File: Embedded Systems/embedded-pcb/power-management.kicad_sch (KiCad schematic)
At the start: 7 parts, among them J2 Screw_Terminal_01x02, U2 LM7805_TO220, U3 LM1117T-3.3

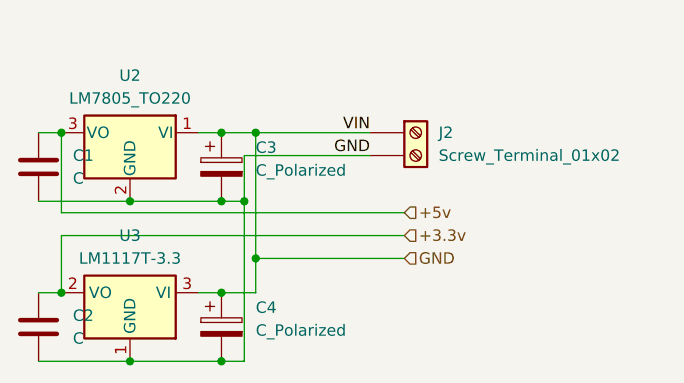
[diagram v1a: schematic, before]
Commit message: feat: finalised PCB
Finalised the electrical design and PCB, including adding a power switch, silksreening, and mounting holes.
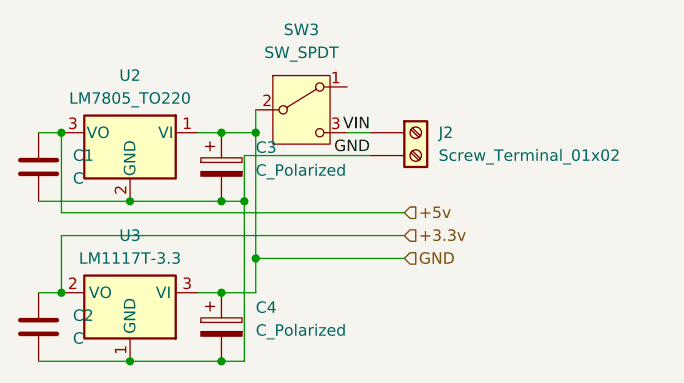
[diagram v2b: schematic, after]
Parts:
- added SW3: SW_SPDT, Connector_Wire:SolderWire-0.1sqmm_1x03_P3.6mm_D0.4mm_OD1mm, symbol Switch:SW_SPDT
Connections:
- net GND: now also SW3.2 (B); no longer J2.1 (Pin_1)
- new net VIN: J2.1 (Pin_1), SW3.3 (C)
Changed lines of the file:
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@@
 		(title "Power Management Circuit")
 		(date "2025-04-06")
-		(rev "v1")
+		(rev "v1.1")
 		(comment 1 "Email: o.meszaros@student.unsw.edu.au")
 		(comment 2 "zID: z5636164")
@@
 	)
 	(junction
+		(at 152.4 73.66)
+		(diameter 0)
+		(color 0 0 0 0)
+	)
+	(junction
 		(at 148.59 81.28)
 		(diameter 0)
@@
 	)
 	(junction
-		(at 152.4 73.66)
-		(diameter 0)
-		(color 0 0 0 0)
-	)
-	(junction
 		(at 130.81 73.66)
 		(diameter 0)
@@
 	(wire
 		(pts
-			(xy 152.4 73.66) (xy 165.1 73.66)
-		)
-		(stroke
-			(width 0)
-			(type default)
-		)
-	)
-	(wire
-		(pts
 			(xy 151.13 99.06) (xy 148.59 99.06)
 		)
@@
 	(wire
 		(pts
+			(xy 162.56 73.66) (xy 165.1 73.66)
+		)
+		(stroke
+			(width 0)
+			(type default)
+		)
+	)
+	(wire
+		(pts
 			(xy 151.13 76.2) (xy 151.13 81.28)
 		)
@@
 		(pts
 			(xy 128.27 73.66) (xy 130.81 73.66)
+		)
+		(stroke
+			(width 0)
+			(type default)
+		)
+	)
+	(wire
+		(pts
+			(xy 152.4 71.12) (xy 152.4 73.66)
 		)
 		(stroke
@@
 					(unit 1)
 				)
+			)
+		)
+	)
+	(symbol
+		(lib_id "Switch:SW_SPDT")
+		(at 157.48 71.12 0)
+		(unit 1)
+		(exclude_from_sim no)
+		(in_bom yes)
+		(on_board yes)
+		(dnp no)
+		(fields_autoplaced yes)
+		(property "Reference" "SW3"
+			(at 157.48 62.23 0)
+			(effects
+				(font
+					(size 1.27 1.27)
+				)
+			)
+		)
+		(property "Value" "SW_SPDT"
+			(at 157.48 64.77 0)
+			(effects
+				(font
+					(size 1.27 1.27)
+				)
+			)
+		)
+		(property "Footprint" "Connector_Wire:SolderWire-0.1sqmm_1x03_P3.6mm_D0.4mm_OD1mm"
+			(at 157.48 71.12 0)
+			(effects
+				(font
+					(size 1.27 1.27)
+				)
+				(hide yes)
+			)
+		)
+		(property "Datasheet" "~"
+			(at 157.48 78.74 0)
+			(effects
+				(font
+					(size 1.27 1.27)
+				)
+				(hide yes)
+			)
+		)
+		(property "Description" "Switch, single pole double throw"
+			(at 157.48 71.12 0)
+			(effects
+				(font
+					(size 1.27 1.27)
+				)
+				(hide yes)
+			)
+		)
+		(pin "1"
+		)
+		(pin "3"
+		)
+		(pin "2"
+		)
+		(instances
+			(project ""
+				(path "/59fd546b-6695-413e-ad86-d6d97541805c/58f26308-bd7c-47be-a3f8-cefe82025330"
+					(reference "SW3")
+					(unit 1)
+				)
